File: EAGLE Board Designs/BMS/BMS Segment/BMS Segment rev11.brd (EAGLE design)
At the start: 108 x 247.1 mm, 269 parts

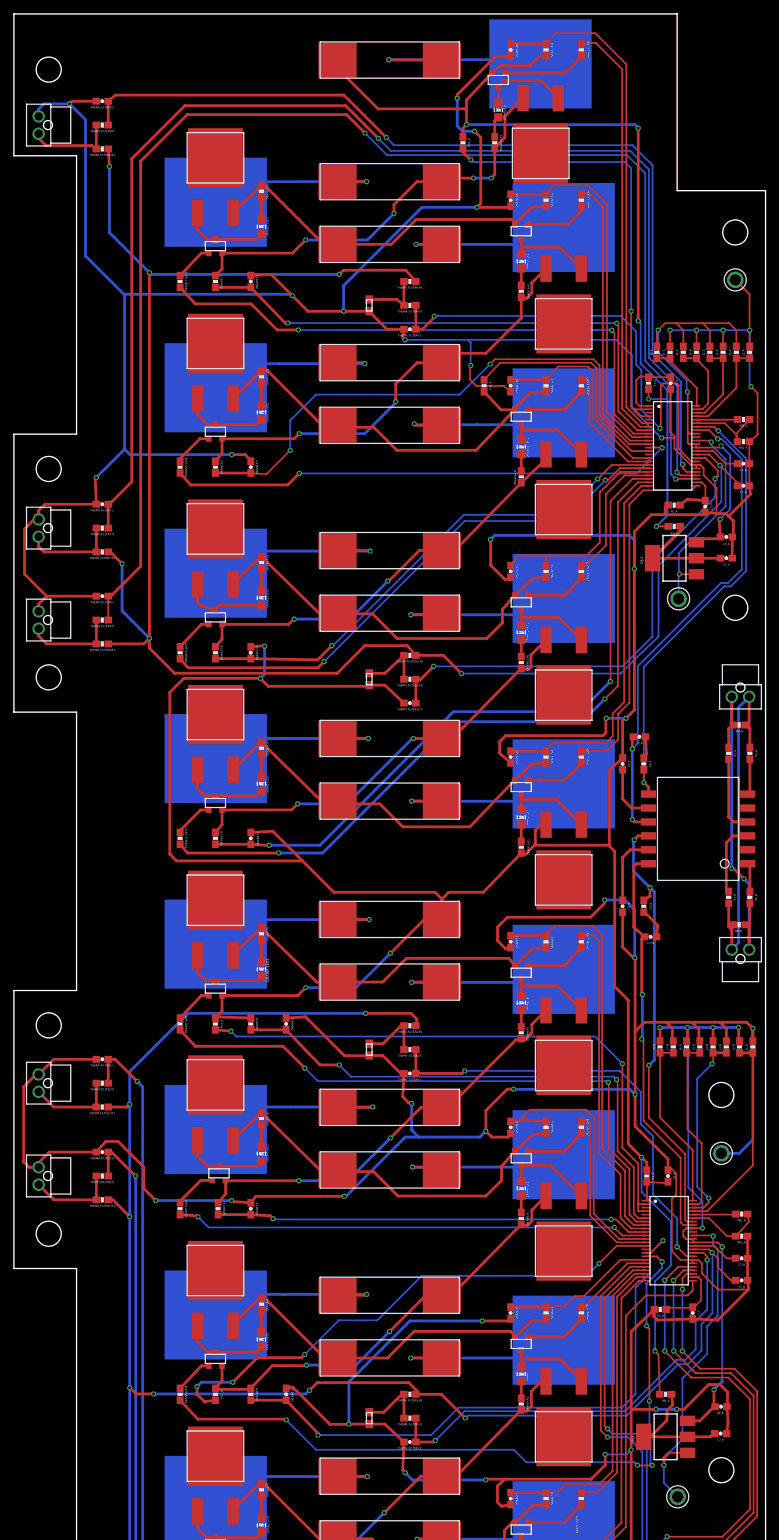
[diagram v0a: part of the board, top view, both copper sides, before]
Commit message: Started adjusting routing
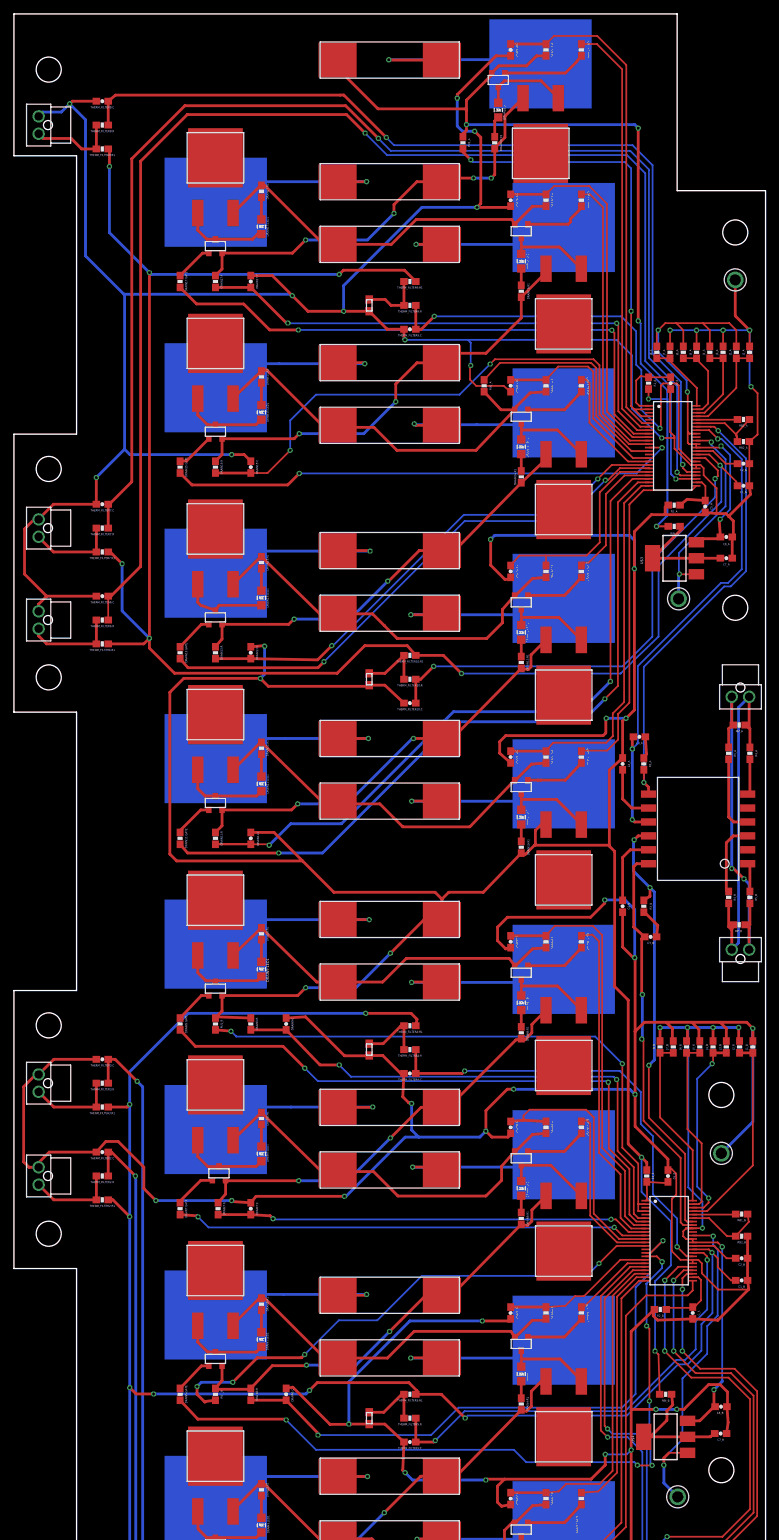
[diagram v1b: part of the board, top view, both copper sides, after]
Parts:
- J1_A, J1_B, J2_A, J2_B, J3_A, J3_B, J4_A, J4_B, J5_A, J5_B, J6_A, J6_B, J7_A, J7_B, J8_A, J8_B: value (none) -> 0
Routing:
- net C2_A: track 99.3 -> 104.5 mm
- net V-_A: track 788.0 -> 786.5 mm
- net SENSE18: track 133.8 -> 132.2 mm
- net V-_B: track 697.8 -> 696.3 mm
- net N$37: track 13.5 -> 12.7 mm
- net SENSE15: track 64.6 -> 63.9 mm

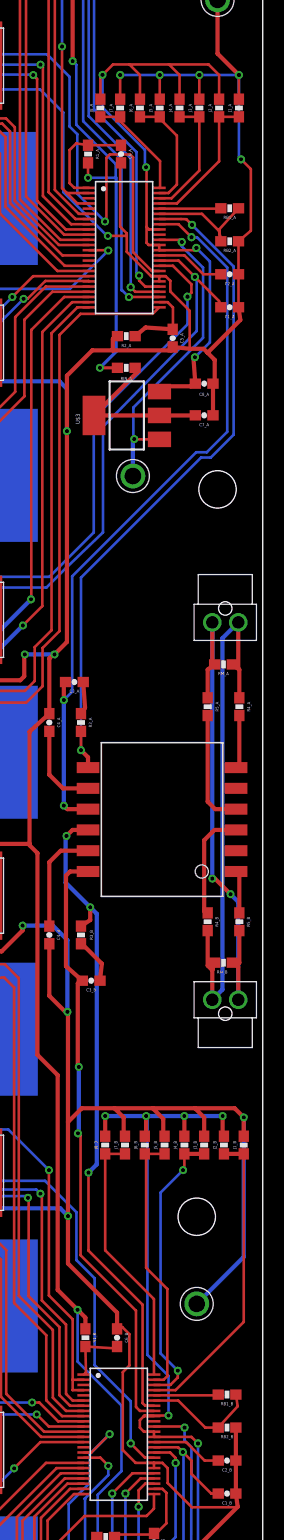
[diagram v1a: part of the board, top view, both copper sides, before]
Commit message: Swapped in LTC6811 Part and added attributes
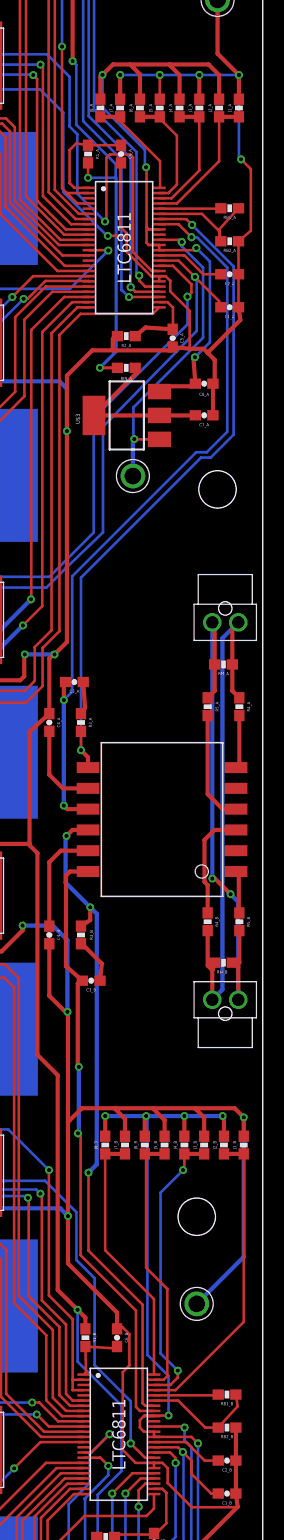
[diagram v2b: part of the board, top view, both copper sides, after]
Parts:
- U$1, U$2: value LTC6804-2 -> LTC6811-2; device HyTechDevices:LTC6804 -> HyTechDevices:LTC6811
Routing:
- net VREG_A: track 67.0 -> 79.0 mm
- net ISOSPI-P: track 54.5 -> 52.8 mm
- net ISOSPI-M: track 52.6 -> 52.1 mm

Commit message: Replaced 6804 references with 6811
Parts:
- J8_B: value 0 -> tolerance

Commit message: Adjusted routing slightly
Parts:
- moved C6_A 0.90 mm to (93.5, 193.9)
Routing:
- net GPIO4_A: track 73.5 -> 60.2 mm
- net V-_A: track 786.5 -> 795.0 mm
- net V+_A: track 10.5 -> 9.19 mm
- net ISOSPI-P: track 52.8 -> 53.6 mm

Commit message: Adjusted silkscreen in progress
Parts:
- ISOSPI_A, ISOSPI_B: value CONNECTOR-2NANO-FIT_VERTICAL-2 -> ISOSPI
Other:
- board text added: "HyTech 2020 BMS Segment rev11 Designed by Arvind Srinivasan, based on rev10 by Yvonne Yeh"
- board text removed: "HyTech 2018 BMS Segment rev11 Designed by Arvind Srinivasan, based on rev10 by Yvonne Yeh"

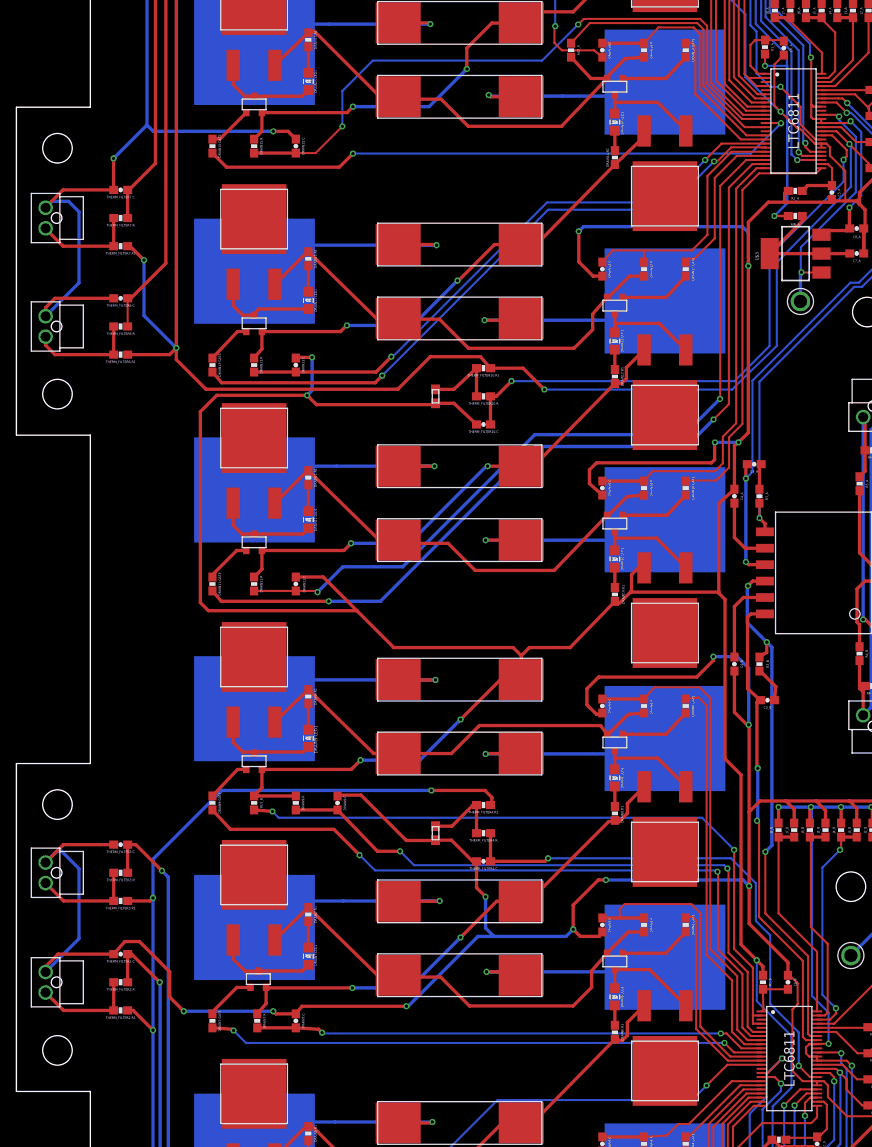
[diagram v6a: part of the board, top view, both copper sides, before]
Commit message: Adjusting BMS silkscreen
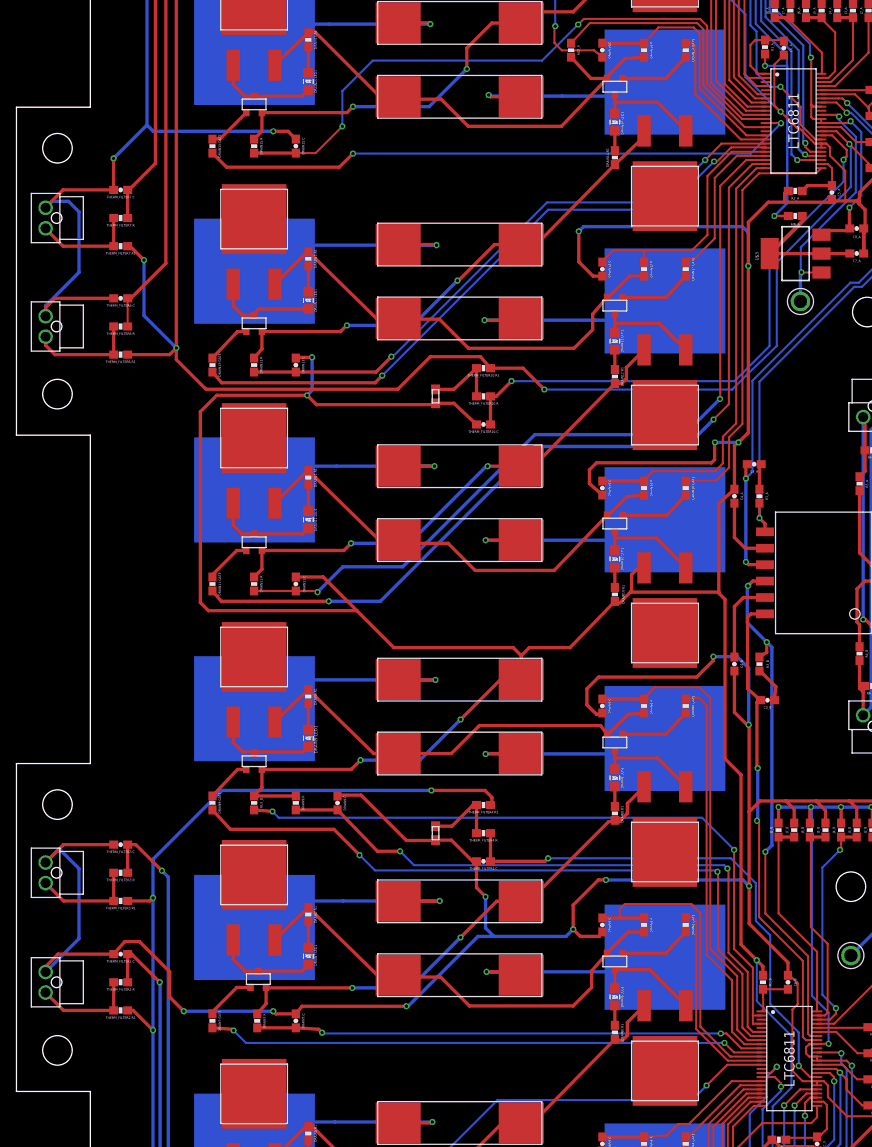
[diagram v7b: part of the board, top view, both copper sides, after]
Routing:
- net C5_B: track 86.9 -> 84.6 mm
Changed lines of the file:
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@@
 <?xml version="1.0" encoding="utf-8"?>
 <!DOCTYPE eagle SYSTEM "eagle.dtd">
-<eagle version="9.5.1">
+<eagle version="9.5.2">
 <drawing>
 <settings>
@@
 <grid distance="50" unitdist="mil" unit="mil" style="lines" multiple="1" display="yes" altdistance="5" altunitdist="mil" altunit="mil"/>
 <layers>
-<layer number="1" name="Top" color="4" fill="1" visible="no" active="yes"/>
+<layer number="1" name="Top" color="4" fill="1" visible="yes" active="yes"/>
 <layer number="2" name="Route2" color="1" fill="3" visible="no" active="no"/>
 <layer number="3" name="Route3" color="4" fill="3" visible="no" active="no"/>
@@
 <layer number="14" name="Route14" color="1" fill="6" visible="no" active="no"/>
 <layer number="15" name="Route15" color="4" fill="6" visible="no" active="no"/>
-<layer number="16" name="Bottom" color="3" fill="1" visible="no" active="yes"/>
+<layer number="16" name="Bottom" color="3" fill="1" visible="yes" active="yes"/>
 <layer number="17" name="Pads" color="2" fill="1" visible="yes" active="yes"/>
 <layer number="18" name="Vias" color="2" fill="1" visible="yes" active="yes"/>
@@
 <layer number="23" name="tOrigins" color="15" fill="1" visible="yes" active="yes"/>
 <layer number="24" name="bOrigins" color="15" fill="1" visible="yes" active="yes"/>
-<layer number="25" name="tNames" color="7" fill="1" visible="no" active="yes"/>
+<layer number="25" name="tNames" color="7" fill="1" visible="yes" active="yes"/>
 <layer number="26" name="bNames" color="7" fill="1" visible="yes" active="yes"/>
 <layer number="27" name="tValues" color="7" fill="1" visible="yes" active="yes"/>
@@
 <layer number="39" name="tKeepout" color="4" fill="11" visible="yes" active="yes"/>
 <layer number="40" name="bKeepout" color="1" fill="11" visible="yes" active="yes"/>
-<layer number="41" name="tRestrict" color="4" fill="10" visible="yes" active="yes"/>
-<layer number="42" name="bRestrict" color="1" fill="10" visible="yes" active="yes"/>
+<layer number="41" name="tRestrict" color="4" fill="10" visible="no" active="yes"/>
+<layer number="42" name="bRestrict" color="1" fill="10" visible="no" active="yes"/>
 <layer number="43" name="vRestrict" color="2" fill="10" visible="no" active="yes"/>
 <layer number="44" name="Drills" color="7" fill="1" visible="no" active="yes"/>
@@
 </element>
 <element name="CELL10" library="HyTechDevices" package="KEYSTONE5222" value="BATTERY_SPRING_KEYSTONE5222" x="79" y="136.48" smashed="yes" rot="MR270">
-<attribute name="NAME" x="84.92" y="136.507" size="2.032" layer="26" font="vector" rot="MR270" align="top-center"/>
+<attribute name="NAME" x="83.82" y="136.507" size="2.032" layer="26" font="vector" rot="MR270" align="top-center"/>
 </element>
 <element name="RU2_A" library="HyTechDevices" package="0603-RES" value="100R" x="67.564" y="193.675" smashed="yes" rot="R90">
@@
 <contactref element="U$2" pad="17"/>
 <wire x1="90.8595" y1="64.6405" x2="93.134" y2="66.915" width="0.254" layer="16"/>
-<wire x1="93.134" y1="66.915" x2="93.134" y2="67.804" width="0.254" layer="16"/>
+<wire x1="93.134" y1="66.915" x2="93.134" y2="67.423" width="0.254" layer="16"/>
 <wire x1="90.78" y1="68.5892" x2="92.372" y2="68.5892" width="0.254" layer="1"/>
 <wire x1="92.372" y1="68.5892" x2="93.134" y2="67.8272" width="0.254" layer="1"/>
-<wire x1="93.134" y1="67.8272" x2="93.134" y2="67.804" width="0.254" layer="1"/>
-<via x="93.134" y="67.804" extent="1-16" drill="0.4"/>
+<wire x1="93.134" y1="67.8272" x2="93.134" y2="67.423" width="0.254" layer="1"/>
+<via x="93.134" y="67.423" extent="1-16" drill="0.4"/>
 <via x="39.116" y="45.085" extent="1-16" drill="0.381"/>
 <wire x1="39.116" y1="45.085" x2="43.4079" y2="40.7931" width="0.254" layer="16"/>
@@
 <contactref element="DRAIN5:C" pad="1"/>
 <wire x1="34.036" y1="47.918" x2="39.116" y2="47.918" width="0.4064" layer="1"/>
-<wire x1="90.78" y1="69.0892" x2="91.4982" y2="69.0892" width="0.254" layer="1"/>
-<wire x1="91.4982" y1="69.0892" x2="93.261" y2="70.852" width="0.254" layer="1"/>
-<via x="93.261" y="70.852" extent="1-16" drill="0.4"/>
-<wire x1="93.261" y1="70.852" x2="91.356" y2="68.947" width="0.254" layer="16"/>
-<wire x1="91.356" y1="68.947" x2="91.356" y2="66.153" width="0.254" layer="16"/>
+<wire x1="90.78" y1="69.0892" x2="91.8792" y2="69.0892" width="0.254" layer="1"/>
+<wire x1="91.8792" y1="69.0892" x2="92.626" y2="69.836" width="0.254" layer="1"/>
+<via x="92.626" y="69.836" extent="1-16" drill="0.4"/>
+<wire x1="92.626" y1="69.836" x2="91.356" y2="68.566" width="0.254" layer="16"/>
+<wire x1="91.356" y1="68.566" x2="91.356" y2="66.153" width="0.254" layer="16"/>
 <wire x1="91.356" y1="66.153" x2="89.324" y2="64.121" width="0.254" layer="16"/>
 <wire x1="89.324" y1="64.121" x2="89.324" y2="48.8148" width="0.254" layer="16"/>
@@
 <wire x1="8.382" y1="234.569" x2="11.85" y2="234.569" width="0.4064" layer="1"/>
 <wire x1="11.85" y1="176.657" x2="5.68155" y2="176.657" width="0.4064" layer="1"/>
-<wire x1="7.62" y1="165.334" x2="3.556" y2="161.27" width="0.4064" layer="16"/>
-<wire x1="5.68155" y1="176.657" x2="3.529275" y2="174.504725" width="0.4064" layer="1"/>
+<wire x1="7.62" y1="166.604" x2="3.556" y2="162.54" width="0.4064" layer="16"/>
+<wire x1="3.556" y1="162.54" x2="3.556" y2="161.27" width="0.4064" layer="16"/>
+<wire x1="5.68155" y1="176.657" x2="4.047275" y2="175.022725" width="0.4064" layer="1"/>
 <wire x1="3.556" y1="174.478" x2="4.338" y2="175.26" width="0.4064" layer="16"/>
 <wire x1="4.338" y1="175.26" x2="6.35" y2="175.26" width="0.4064" layer="16"/>
 <wire x1="6.35" y1="175.26" x2="7.62" y2="173.99" width="0.4064" layer="16"/>
-<wire x1="7.62" y1="173.99" x2="7.62" y2="165.334" width="0.4064" layer="16"/>
+<wire x1="7.62" y1="173.99" x2="7.62" y2="166.604" width="0.4064" layer="16"/>
 <wire x1="99.5066" y1="175.3132" x2="99.3316" y2="175.4882" width="0.4064" layer="1"/>
 <wire x1="100.965" y1="175.3132" x2="99.5066" y2="175.3132" width="0.4064" layer="1"/>
@@
 <wire x1="71.374" y1="166.155" x2="70.2428" y2="166.155" width="0.4064" layer="1"/>
 <wire x1="70.2428" y1="166.155" x2="68.5038" y2="167.894" width="0.4064" layer="1"/>
-<wire x1="3.529275" y1="174.504725" x2="3.556" y2="174.478" width="0" layer="19" extent="1-1"/>
+<wire x1="3.556" y1="174.478" x2="3.556" y2="174.53145" width="0.3048" layer="1"/>
+<wire x1="3.556" y1="174.53145" x2="4.047275" y2="175.022725" width="0.3048" layer="1"/>
 </signal>
 <signal name="V+_A">
@@
 <contactref element="THERM_FILTER7:R" pad="1"/>
 <contactref element="THERM_FILTER7:C" pad="1"/>
-<wire x1="98.038" y1="180.8004" x2="95.7296" y2="180.8004" width="0.254" layer="1"/>
+<wire x1="98.038" y1="180.8004" x2="96.52" y2="180.8004" width="0.254" layer="1"/>
 <wire x1="24.554" y1="233.92" x2="16.934" y2="226.3" width="0.4064" layer="1"/>
 <wire x1="47.668" y1="233.92" x2="24.554" y2="233.92" width="0.4064" layer="1"/>
 <wire x1="52.367" y1="229.221" x2="47.668" y2="233.92" width="0.4064" layer="1"/>
 <wire x1="91.251" y1="224.744" x2="88.557" y2="227.438" width="0.254" layer="16"/>
-<wire x1="95.7296" y1="180.8004" x2="95.293" y2="181.237" width="0.254" layer="1"/>
-<via x="95.293" y="181.237" extent="1-16" drill="0.4"/>
-<wire x1="95.293" y1="181.237" x2="95.293" y2="193.661" width="0.254" layer="16"/>
+<wire x1="95.293" y1="181.61" x2="95.293" y2="193.661" width="0.254" layer="16"/>
 <wire x1="95.293" y1="193.661" x2="91.251" y2="197.703" width="0.254" layer="16"/>
 <wire x1="91.251" y1="197.703" x2="91.251" y2="224.744" width="0.254" layer="16"/>
@@
 <wire x1="16.934" y1="179.8828" x2="13.725" y2="176.6738" width="0.4064" layer="1"/>
 <wire x1="13.55" y1="176.657" x2="13.725" y2="176.6738" width="0.4064" layer="1"/>
+<wire x1="96.52" y1="180.8004" x2="96.2380875" y2="180.8004" width="0.3048" layer="1"/>
+<wire x1="96.2380875" y1="180.8004" x2="96.0649875" y2="180.9735" width="0.3048" layer="1"/>
+<via x="96.0649875" y="180.9735" extent="1-16" drill="0.381"/>
+<wire x1="96.0649875" y1="180.9735" x2="95.9295" y2="180.9735" width="0.3048" layer="16"/>
+<wire x1="95.9295" y1="180.9735" x2="95.293" y2="181.61" width="0.3048" layer="16"/>
 </signal>
 <signal name="IP_A">

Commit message: Cleaned up silkscreen and board
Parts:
- moved J1_B 1.27 mm to (106.2, 97.4)
- moved J2_B 1.27 mm to (104.3, 97.4)
- moved J3_B 1.27 mm to (102.4, 97.4)
- moved J4_B 1.27 mm to (100.5, 97.4)
- moved J5_B 1.27 mm to (98.6, 97.4)
- moved J6_B 1.27 mm to (96.6, 97.4)
- moved J7_B 1.27 mm to (94.7, 97.4)
- moved J8_B 1.27 mm to (92.8, 97.4)
- moved R1_A 0.76 mm to (90.4, 194.1)
- moved U$7 0.13 mm to (95.5, 34.0)
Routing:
- net V-_B: track 696.8 -> 695.0 mm
- net N$9: track 25.6 -> 24.3 mm
- net N$8: track 25.1 -> 23.8 mm
- net N$16: track 29.4 -> 28.2 mm
- net N$13: track 27.6 -> 26.4 mm
- net VREG_B: track 88.5 -> 87.3 mm
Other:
- board text added: "Cell 0"
- board text added: "Cell 18"
- board text removed: "Cell 0 NEG"
